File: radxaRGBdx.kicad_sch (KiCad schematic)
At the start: 67 parts, among them J1 Conn_02x20_Odd_Even

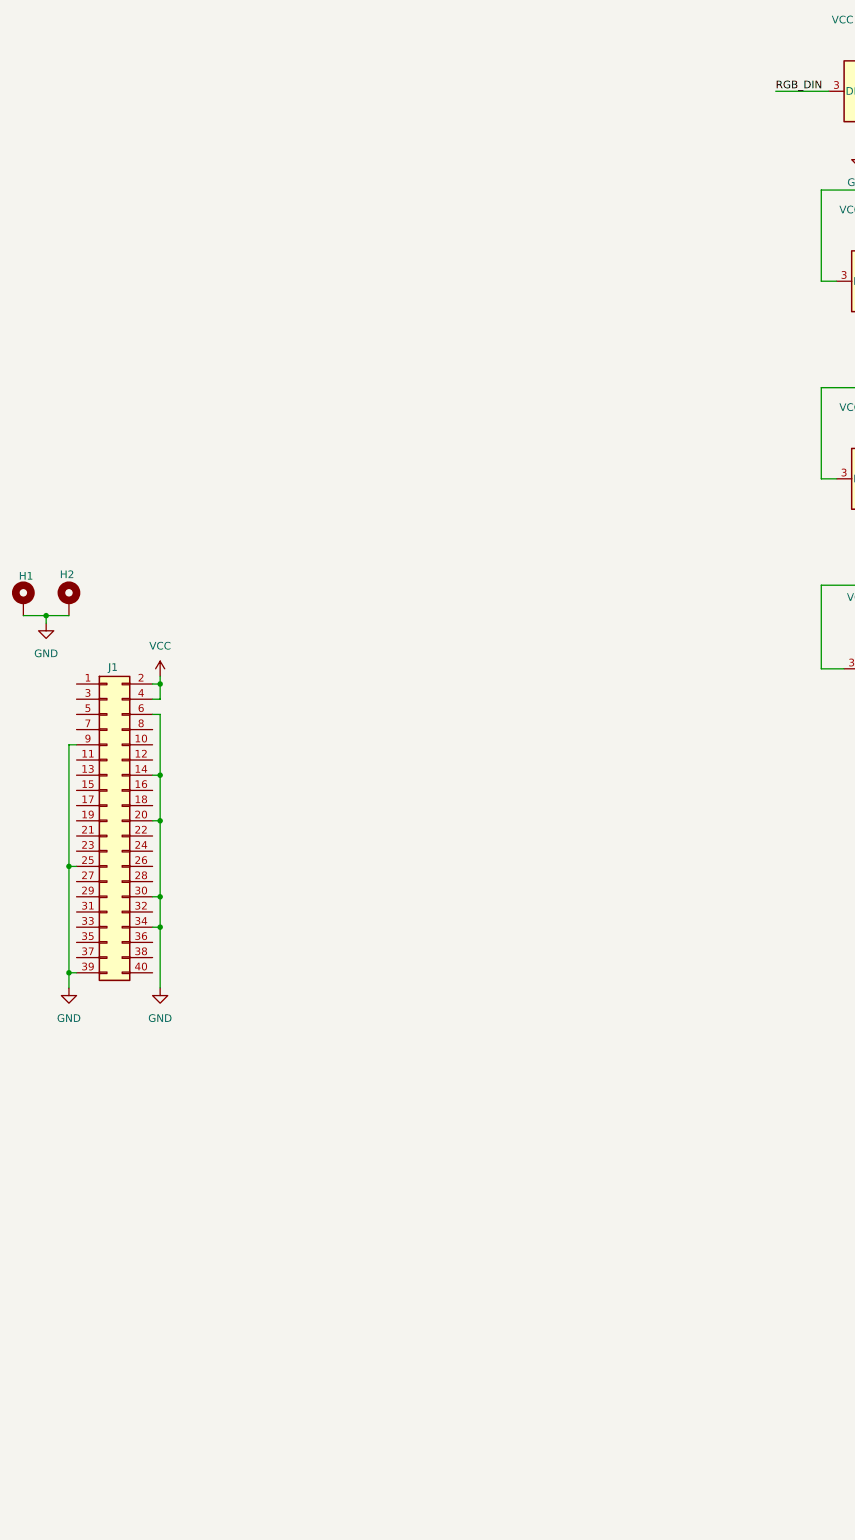
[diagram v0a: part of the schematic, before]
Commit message: Routing work, added level shifters / MCU / IMU, routed power / signals
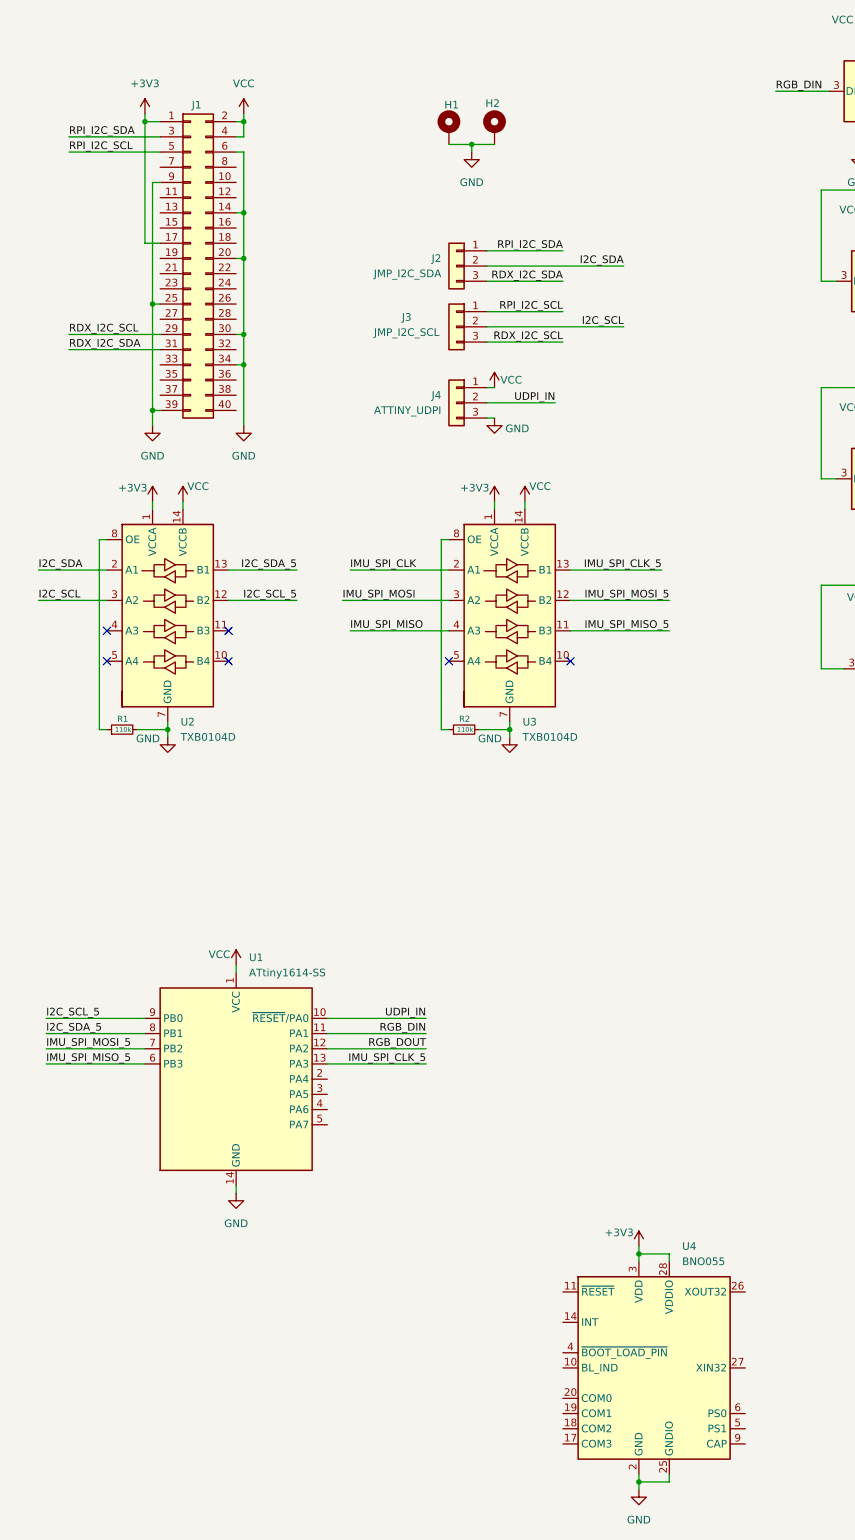
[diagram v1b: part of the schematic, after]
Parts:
- added J2: JMP_I2C_SDA, Connector_PinHeader_1.27mm:PinHeader_1x03_P1.27mm_Vertical, symbol Connector_Generic:Conn_01x03
- added J3: JMP_I2C_SCL, Connector_PinHeader_1.27mm:PinHeader_1x03_P1.27mm_Vertical, symbol Connector_Generic:Conn_01x03
- added J4: ATTINY_UDPI, Connector_PinHeader_2.54mm:PinHeader_1x03_P2.54mm_Vertical, symbol Connector_Generic:Conn_01x03
- added R1, R2: 110k, PCM_Resistor_SMD_AKL:R_1206_3216Metric_Pad1.42x1.75mm_HandSolder, symbol Device:R_Small
- added U1: ATtiny1614-SS, Package_SO:SOIC-14_3.9x8.7mm_P1.27mm, symbol MCU_Microchip_ATtiny:ATtiny1614-SS
- added U2, U3: TXB0104D, Package_SO:SOIC-14_3.9x8.7mm_P1.27mm, symbol Logic_LevelTranslator:TXB0104D
- added U4: BNO055, Package_LGA:LGA-28_5.2x3.8mm_P0.5mm, symbol Sensor_Motion:BNO055
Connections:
- net GND: now also J4.3 (Pin_3), R1.2, R2.2, U1.14 (GND), U2.7 (GND), U3.7 (GND), U4.2 (GND), U4.25 (GNDIO)
- net RGB_DIN: now also U1.11 (PA1)
- net RGB_DOUT: now also U1.12 (PA2)
- net VCC: now also J4.1 (Pin_1), U1.1 (VCC), U2.14 (VCCB), U3.14 (VCCB)
- net +3V3: now reaches J1.1 (Pin_1)
- net +3V3: now also J1.17 (Pin_17), U2.1 (VCCA), U3.1 (VCCA), U4.28 (VDDIO), U4.3 (VDD)
- net RDX_I2C_SCL: now reaches J1.29 (Pin_29)
- net RDX_I2C_SCL: now also J3.3 (Pin_3)
- net RPI_I2C_SDA: now reaches J1.3 (Pin_3)
- net RPI_I2C_SDA: now also J2.1 (Pin_1)
- net RDX_I2C_SDA: now reaches J1.31 (Pin_31)
- net RDX_I2C_SDA: now also J2.3 (Pin_3)
- net RPI_I2C_SCL: now reaches J1.5 (Pin_5)
- net RPI_I2C_SCL: now also J3.1 (Pin_1)
- new net: R2.1, U3.8 (OE)
- new net: R1.1, U2.8 (OE)
- new net I2C_SCL: J3.2 (Pin_2), U2.3 (A2)
- new net I2C_SCL_5: U1.9 (PB0), U2.12 (B2)
- new net I2C_SDA: J2.2 (Pin_2), U2.2 (A1)
- new net I2C_SDA_5: U1.8 (PB1), U2.13 (B1)
- new net IMU_SPI_CLK: U3.2 (A1)
- new net IMU_SPI_CLK_5: U1.13 (PA3), U3.13 (B1)
- new net IMU_SPI_MISO: U3.4 (A3)
- new net IMU_SPI_MISO_5: U1.6 (PB3), U3.11 (B3)
- new net IMU_SPI_MOSI: U3.3 (A2)
- new net IMU_SPI_MOSI_5: U1.7 (PB2), U3.12 (B2)
- new net UDPI_IN: J4.2 (Pin_2), U1.10 (~{RESET}/PA0)
- no-connect marks 0 -> 6
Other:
- moved on the sheet: H1, H2, J1
